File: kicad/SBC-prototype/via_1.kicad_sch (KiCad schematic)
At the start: 1 part, among them IC5 W65C22S6TPG-14

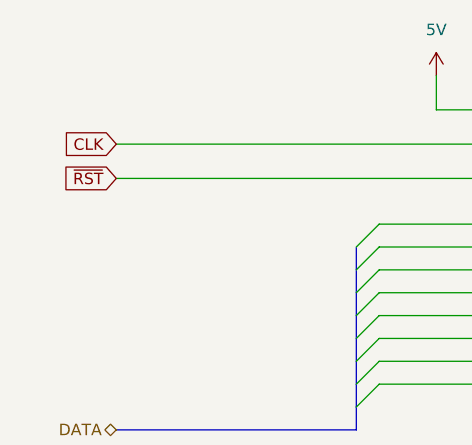
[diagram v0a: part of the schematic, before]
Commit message: Started including hierarchical flow in the top level sheet
- First, hierarchical designs - I don't need a schematic to all fit on
  one sheet.
- I had the clock and reset lines as global labels, so I converted them
  to hierarchical labels instead, imported them on each sheet, and then
  connected the sheets together. It probably looks like overkill right
  now, but it will allow me to modify each block more easily
- The VIA has unconnected ports for now because I haven't wired them to
  anything on the prototyep in the lab yet. That's next, once the
  EEPROM, SRAM, and address decoders are all working (and VIA1 doesn't
  need a load except for maybe some resistors for now).
- Finally, the power rails and ground are global labels right now and
  aren't connected to anything on the top level design schematic. I'm
  not sure if that's normal, so for now I've just left them.
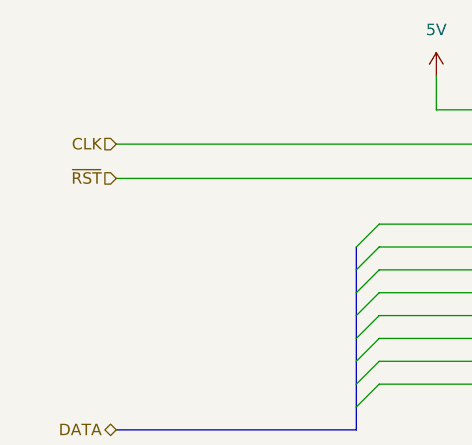
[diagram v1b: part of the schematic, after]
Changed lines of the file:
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@@
 	(title_block
 		(title "65C02 Single Board Computer")
+		(rev "Proto")
 	)
 	(bus_entry
@@
 			(width 0)
 			(type default)
-		)
-	)
-	(global_label "~{RST}"
-		(shape input)
-		(at 88.9 78.74 180)
-		(fields_autoplaced yes)
-		(effects
-			(font
-				(size 1.27 1.27)
-			)
-			(justify right)
-		)
-		(property "Intersheetrefs" "${INTERSHEET_REFS}"
-			(at 82.4677 78.74 0)
-			(effects
-				(font
-					(size 1.27 1.27)
-				)
-				(justify right)
-				(hide yes)
-			)
-		)
-	)
-	(global_label "CLK"
-		(shape input)
-		(at 88.9 74.93 180)
-		(fields_autoplaced yes)
-		(effects
-			(font
-				(size 1.27 1.27)
-			)
-			(justify right)
-		)
-		(property "Intersheetrefs" "${INTERSHEET_REFS}"
-			(at 82.3467 74.93 0)
-			(effects
-				(font
-					(size 1.27 1.27)
-				)
-				(justify right)
-				(hide yes)
-			)
 		)
 	)
@@
 		(shape input)
 		(at 88.9 116.84 180)
+		(fields_autoplaced yes)
+		(effects
+			(font
+				(size 1.27 1.27)
+			)
+			(justify right)
+		)
+	)
+	(hierarchical_label "~{RST}"
+		(shape input)
+		(at 88.9 78.74 180)
+		(fields_autoplaced yes)
+		(effects
+			(font
+				(size 1.27 1.27)
+			)
+			(justify right)
+		)
+	)
+	(hierarchical_label "CLK"
+		(shape input)
+		(at 88.9 74.93 180)
 		(fields_autoplaced yes)
 		(effects
@@
 					(reference "IC5")
 					(unit 1)
-				)
-				(path "/1c8fb460-190a-4823-a6aa-9b1d397d6158/0456201c-b4b8-4a85-8590-2dcf9ac729a4"
-					(reference "IC5")
-					(unit 1)

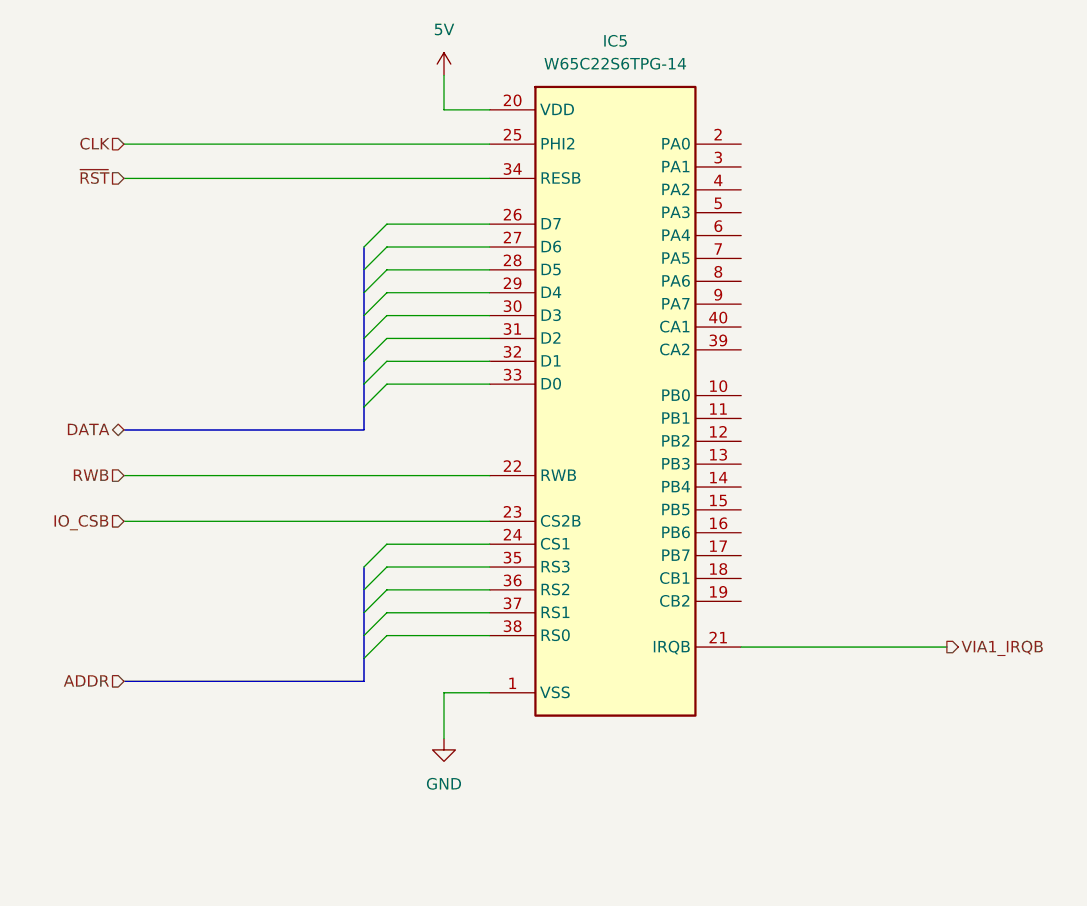
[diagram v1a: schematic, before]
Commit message: Fixed a ton of DRC errors and warnings
- VIA 1 is still unconnected since it's on the breadboard that way and I
  haven't hooked it to anything yet
- All the parts in the library have changed because I've modified my own
  versions of them. I'm not sure if I should add my changes to the
  library or find a way to tell the tool that it's OK that those are
  updated.
- The 74HC00 NAND gate was completely broken and would have been an
  interesting problem to sort out during routing and placement
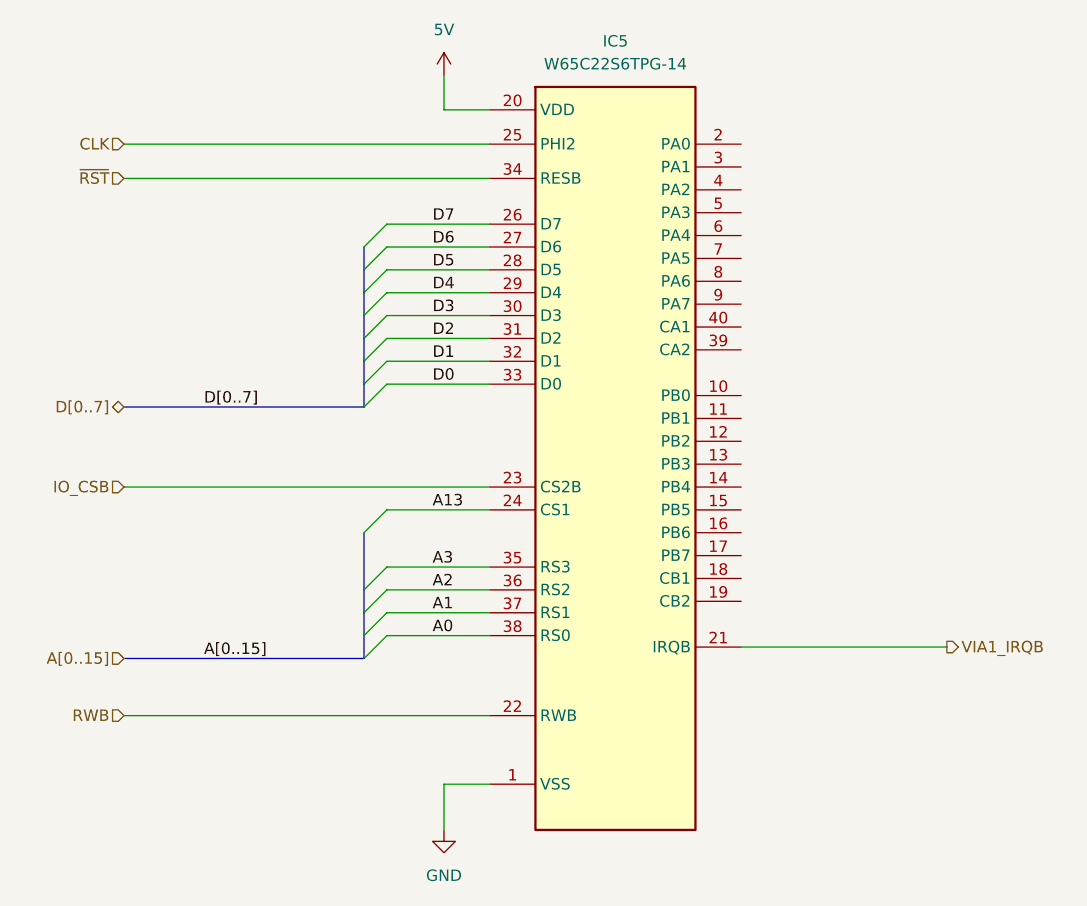
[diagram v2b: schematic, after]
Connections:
- net A13: now reaches IC5.24 (CS1)
- net D7: now reaches IC5.26 (D7)
- net D6: now reaches IC5.27 (D6)
- net D5: now reaches IC5.28 (D5)
- net D4: now reaches IC5.29 (D4)
- net D3: now reaches IC5.30 (D3)
- net D2: now reaches IC5.31 (D2)
- net D1: now reaches IC5.32 (D1)
- net D0: now reaches IC5.33 (D0)
- net A3: now reaches IC5.35 (RS3)
- net A2: now reaches IC5.36 (RS2)
- net A1: now reaches IC5.37 (RS1)
- net A0: now reaches IC5.38 (RS0)
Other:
- moved on the sheet: IC5
